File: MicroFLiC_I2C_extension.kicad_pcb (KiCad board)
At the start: 2 copper layers, 49.8 x 49.8 mm, 13 parts, among them P1 Header_1x14, P2 Socket_1x14, P3 8-188275-4, P4 Header_1x4, P5 Socket_1x4, P6 DB15-VGA, P7 RJ45, SW1 SW_PUSH, SW2 DIPS_04

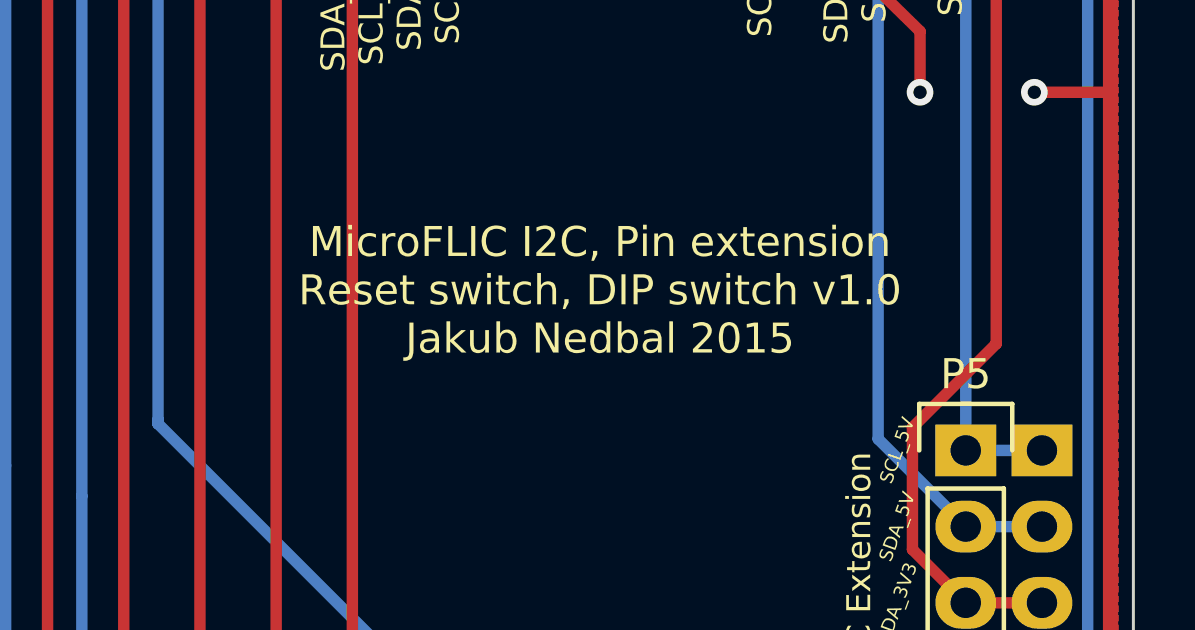
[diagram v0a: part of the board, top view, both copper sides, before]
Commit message: Filled in component details, update board to v1.1
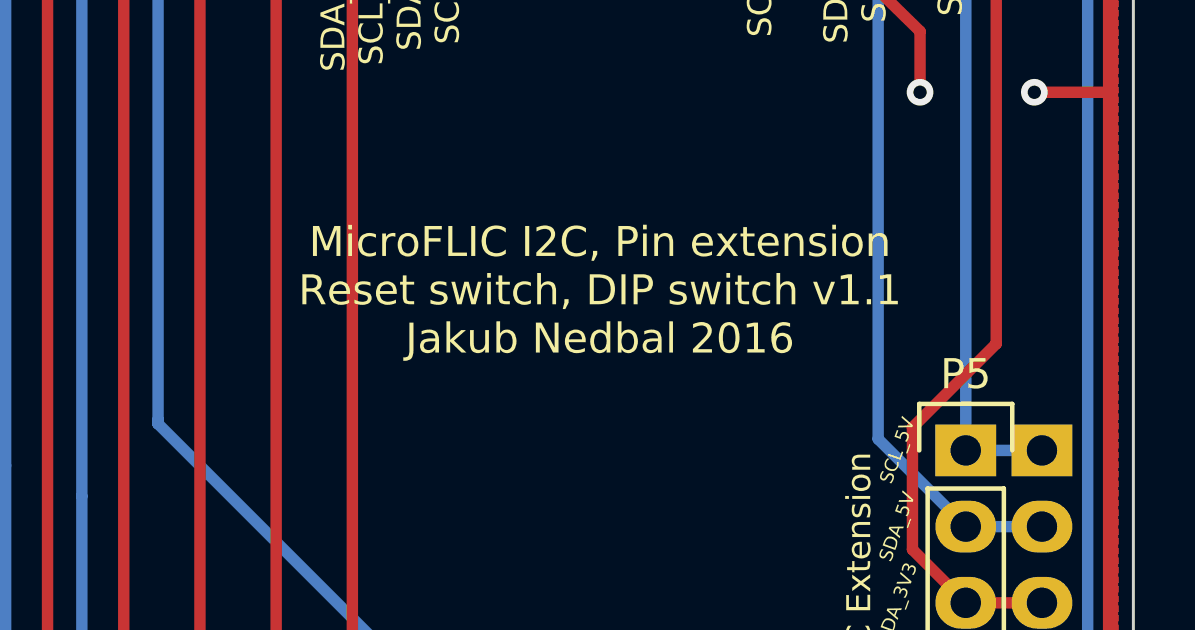
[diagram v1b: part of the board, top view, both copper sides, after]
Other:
- board text added: "MicroFLIC I2C, Pin extension Reset switch, DIP switch v1.1 Jakub Nedbal 2016"
- board text removed: "MicroFLIC I2C, Pin extension Reset switch, DIP switch v1.0 Jakub Nedbal 2015"
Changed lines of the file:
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@@
-(kicad_pcb (version 4) (host pcbnew 4.0.0-2.201512091501+6195~38~ubuntu14.04.1-stable)
+(kicad_pcb (version 4) (host pcbnew "(2015-12-10 BZR 6367)-product")
   (general
     (links 70)
@@
     (effects (font (size 0.8 0.8) (thickness 0.12)) (justify right))
   )
-  (gr_text "MicroFLIC I2C, Pin extension\nReset switch, DIP switch v1.0\nJakub Nedbal 2015" (at 132.08 126.238) (layer F.SilkS)
+  (gr_text "MicroFLIC I2C, Pin extension\nReset switch, DIP switch v1.1\nJakub Nedbal 2016" (at 132.08 126.238) (layer F.SilkS)
     (effects (font (size 1 1) (thickness 0.15)))
   )

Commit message: Fixed connector descriptions
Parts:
- P1: value Header_1x14 -> 1x14 header strip
- P2: value Socket_1x14 -> 1x14 socket strip
- P3: value 8-188275-4 -> 14-way Micro-MaTch
- P4: value Header_1x4 -> 1x4 header strip
- P5: value Socket_1x4 -> 1x4 socket strip
- SW1: value SW_PUSH -> Tactile switch R/A
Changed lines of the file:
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@@
     (links 70)
     (no_connects 0)
-    (area 99.001476 87.834999 151.474334 154.757001)
+    (area 100.025999 100.025999 149.910001 149.910001)
     (thickness 1.6)
     (drawings 84)
@@
   (page A4)
   (layers
-    (0 F.Cu signal hide)
-    (31 B.Cu signal hide)
+    (0 F.Cu signal)
+    (31 B.Cu signal)
     (32 B.Adhes user)
     (33 F.Adhes user)
@@
       (effects (font (size 0.8 0.8) (thickness 0.12)))
     )
-    (fp_text value SW_PUSH (at 0 2.54 180) (layer F.SilkS) hide
+    (fp_text value "Tactile switch R/A" (at 0 2.54 180) (layer F.SilkS) hide
       (effects (font (size 1 1) (thickness 0.15)))
     )
@@
       (effects (font (size 1 1) (thickness 0.15)) (justify mirror))
     )
-    (fp_text value Header_1x14 (at 0 3.1 180) (layer B.Fab) hide
+    (fp_text value "1x14 header strip" (at 0 3.1 180) (layer B.Fab) hide
       (effects (font (size 1 1) (thickness 0.15)) (justify mirror))
     )
@@
       (effects (font (size 1 1) (thickness 0.12)))
     )
-    (fp_text value Socket_1x14 (at 0 -3.1) (layer F.Fab) hide
+    (fp_text value "1x14 socket strip" (at 0 -3.1) (layer F.Fab) hide
       (effects (font (size 1 1) (thickness 0.15)))
     )
@@
       (effects (font (size 1 1) (thickness 0.15)))
     )
-    (fp_text value 8-188275-4 (at -10.795 0 90) (layer F.SilkS) hide
+    (fp_text value "14-way Micro-MaTch" (at -10.795 0 90) (layer F.SilkS) hide
       (effects (font (size 1 1) (thickness 0.15)))
     )
@@
       (effects (font (size 1 1) (thickness 0.15)) (justify mirror))
     )
-    (fp_text value Header_1x4 (at 0 3.1 180) (layer B.Fab) hide
+    (fp_text value "1x4 header strip" (at 0 3.1 180) (layer B.Fab) hide
       (effects (font (size 1 1) (thickness 0.15)) (justify mirror))
     )
@@
       (effects (font (size 1 1) (thickness 0.15)))
     )
-    (fp_text value Socket_1x4 (at 0 -3.1 270) (layer F.Fab) hide
-      (effects (font (size 1 1) (thickness 0.15)))
-    )
+    (fp_text value "1x4 socket strip" (at 0 -3.1 270) (layer F.Fab) hide
+      (effects (font (size 1 1) (thickness 0.15)))
+    )
